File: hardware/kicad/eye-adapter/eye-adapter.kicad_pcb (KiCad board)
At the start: 2 copper layers, 42 x 30 mm, 9 parts, among them J11 vom Mainboard J7, J12 GC9A01 links, J13 GC9A01 rechts

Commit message: Session 2026-10-03 00:27: Reserve raus (Stepper, C3, GPIO45, 7 Loetjumper), alle drei Platinen neu geroutet; Push und Falle 18 behoben
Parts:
- removed C19: 1u, C_Disc_D5.0mm_W2.5mm_P5.00mm
- removed R17: 10k, R_Axial_DIN0207_L6.3mm_D2.5mm_P7.62mm_Horizontal
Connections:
- J11 pad 10: GND -> DISP_RST
- J12 pad 5: EYE_RST -> DISP_RST
- J13 pad 5: EYE_RST -> DISP_RST
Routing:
- net EYE_RST: track 47.2 -> 0.00 mm
- net DISP_RST: track 0.00 -> 44.7 mm
- net GND: track 82.2 -> 59.4 mm
- net 3V3: track 77.2 -> 59.4 mm
- net SPI_MOSI: track 52.5 -> 45.8 mm
- net SPI_SCK: track 47.1 -> 50.7 mm
- net CS_EYE_R: track 23.6 -> 27.0 mm

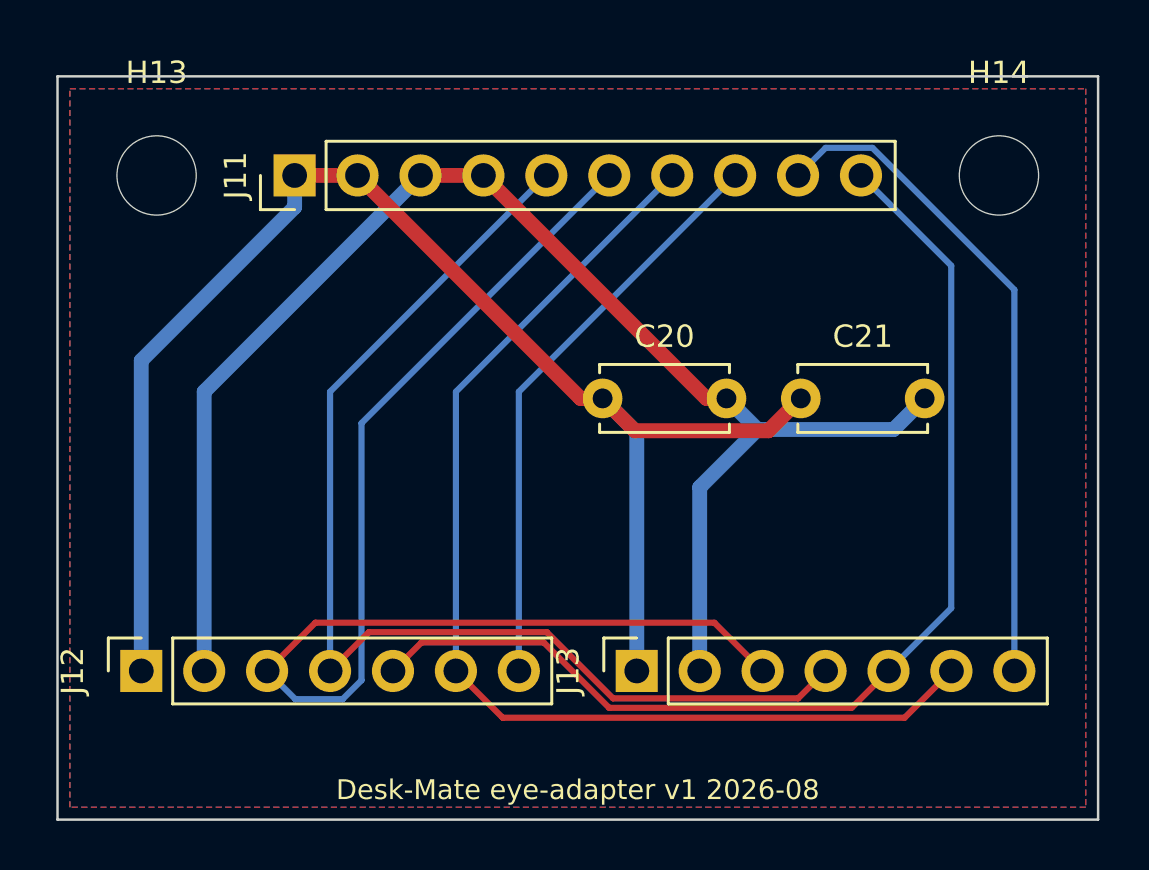
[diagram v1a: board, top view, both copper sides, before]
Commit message: Session 2026-10-09 11:37: Platinen finalisiert: Teile von Reichelt, Silkscreen mit Logo und Pin-Namen, alle drei Boards neu geroutet
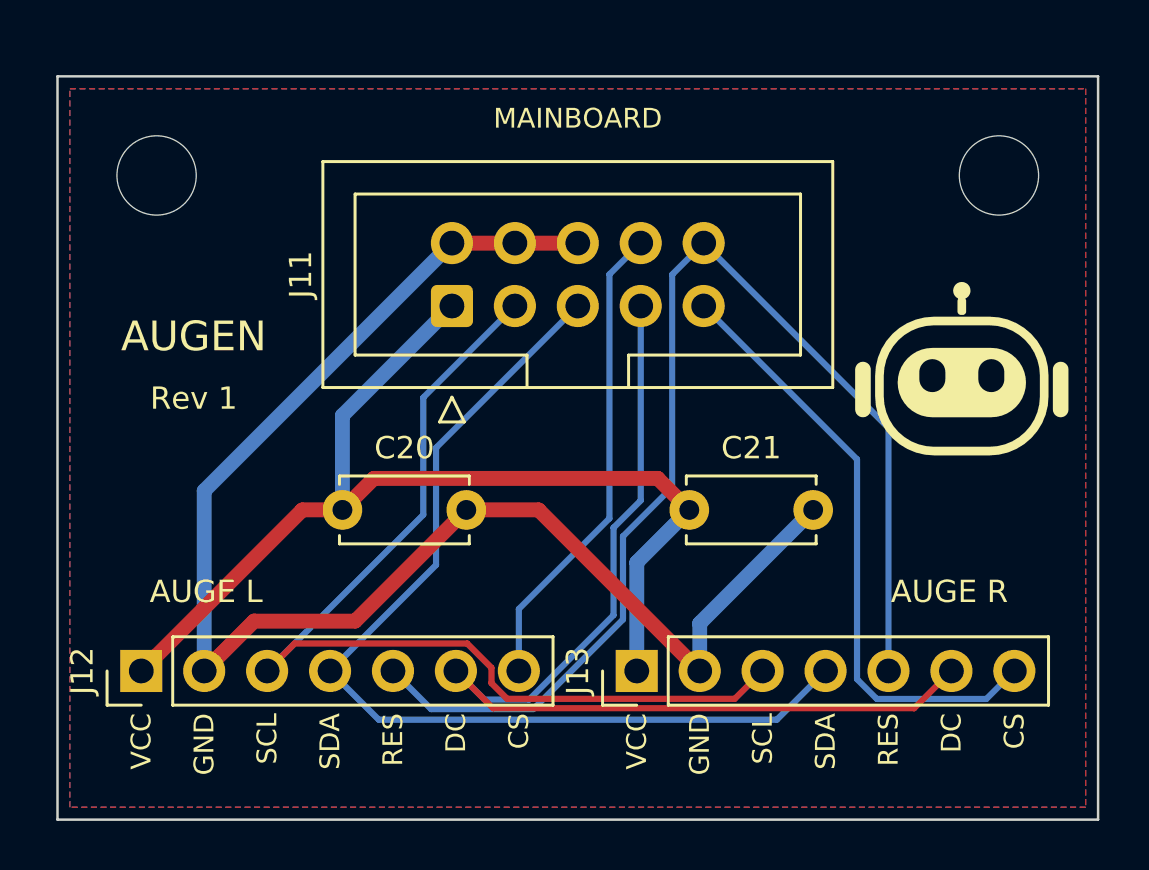
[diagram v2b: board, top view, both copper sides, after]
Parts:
- J11: value vom Mainboard J7 -> IDC 2x5 vom Mainboard J7; footprint PinHeader_1x10_P2.54mm_Vertical -> IDC-Header_2x05_P2.54mm_Vertical
- J12: value GC9A01 links -> GC9A01 links (Dupont); footprint PinSocket_1x07_P2.54mm_Vertical -> PinHeader_1x07_P2.54mm_Vertical
- J13: value GC9A01 rechts -> GC9A01 rechts (Dupont); footprint PinSocket_1x07_P2.54mm_Vertical -> PinHeader_1x07_P2.54mm_Vertical
- moved C20 11.4 mm to (11.5, 17.5)
- moved J11 8.25 mm to (15.9, 9.27)
- moved C21 6.36 mm to (25.5, 17.5)
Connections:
- J11 pad 2: 3V3 -> GND
- J11 pad 3: GND -> SPI_SCK
- J11 pad 6: SPI_SCK -> GND
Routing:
- net 3V3: track 59.4 -> 43.3 mm
- net SPI_SCK: track 50.7 -> 41.1 mm
- net SPI_MOSI: track 45.8 -> 40.5 mm
- net CS_EYE_L: track 23.6 -> 19.3 mm
- net DISP_RST: track 44.7 -> 48.3 mm
- net SPI_DC: track 45.2 -> 42.4 mm
- net CS_EYE_R: track 27.0 -> 24.8 mm
- net GND: track 59.4 -> 60.3 mm
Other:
- board text added: "AUGE L"
- board text added: "AUGE R"
- board text added: "AUGEN"
- board text added: "CS"
- board text added: "DC"
- board text added: "GND"
- board text added: "JLCJLCJLCJLC"
- board text added: "MAINBOARD"
- board text added: "RES"
- board text added: "Rev 1"
- board text added: "SCL"
- board text added: "SDA"
- board text added: "VCC"
- board text removed: "Desk-Mate eye-adapter v1 2026-08"
